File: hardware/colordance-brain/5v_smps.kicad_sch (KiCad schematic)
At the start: 15 parts, among them J14 Anderson, U8 AP3211

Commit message: Start updating brain for v1.2
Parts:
- J14: footprint homebrew:Anderson_1336G1_right_angle_bottom_two -> Homebrew:Anderson_1336G1_right_angle_bottom_two
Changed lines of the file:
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@@
       (effects (font (size 1.524 1.524)))
     )
-    (property "Footprint" "homebrew:Anderson_1336G1_right_angle_bottom_two" (id 2) (at 33.02 50.8 0)
+    (property "Footprint" "Homebrew:Anderson_1336G1_right_angle_bottom_two" (id 2) (at 33.02 50.8 0)
       (effects (font (size 1.524 1.524)) hide)
     )

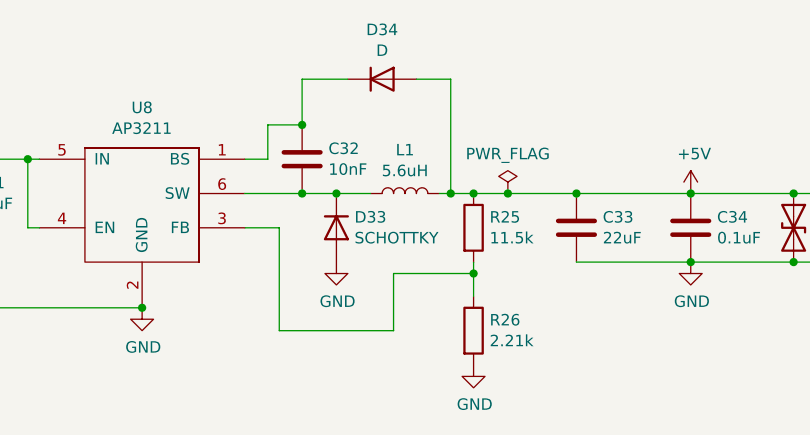
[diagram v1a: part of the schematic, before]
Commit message: Update colordance-brain PCB files to KiCAD 7
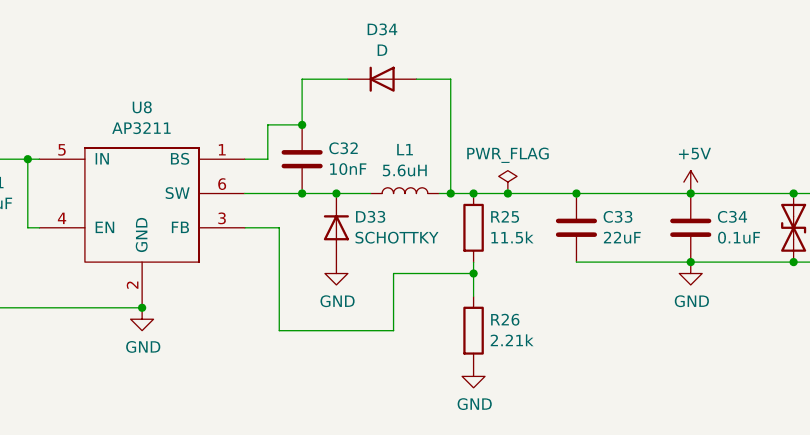
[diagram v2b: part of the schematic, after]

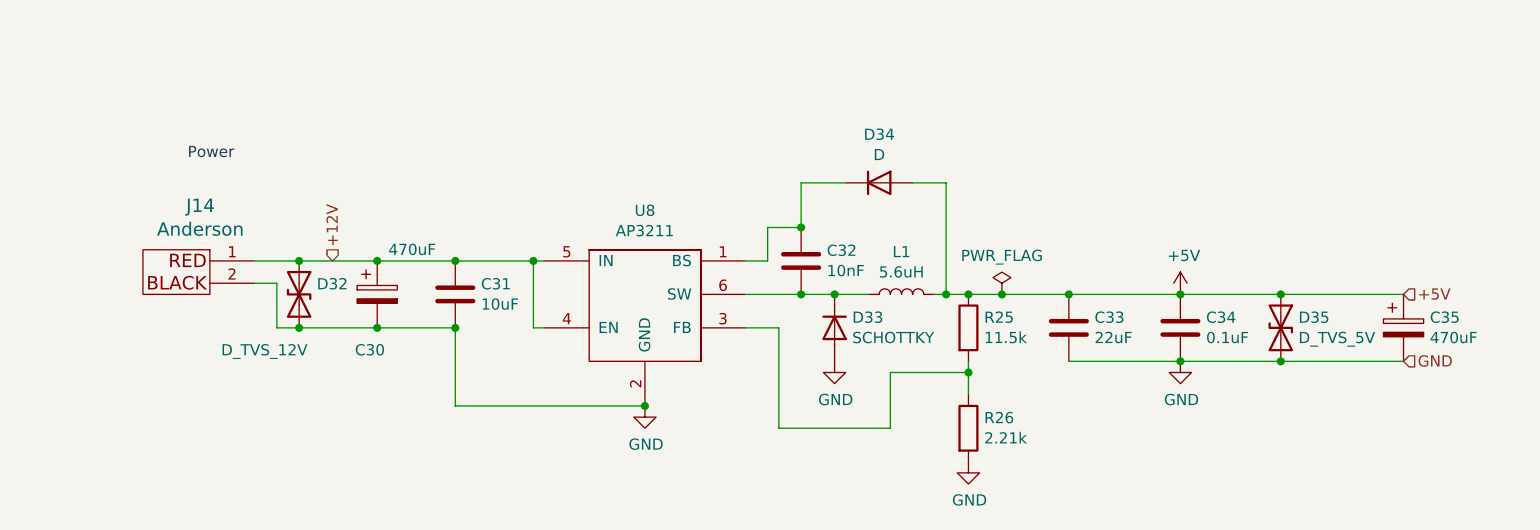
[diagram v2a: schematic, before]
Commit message: Update colordance-brain schematic for v1.3: JLC assembly
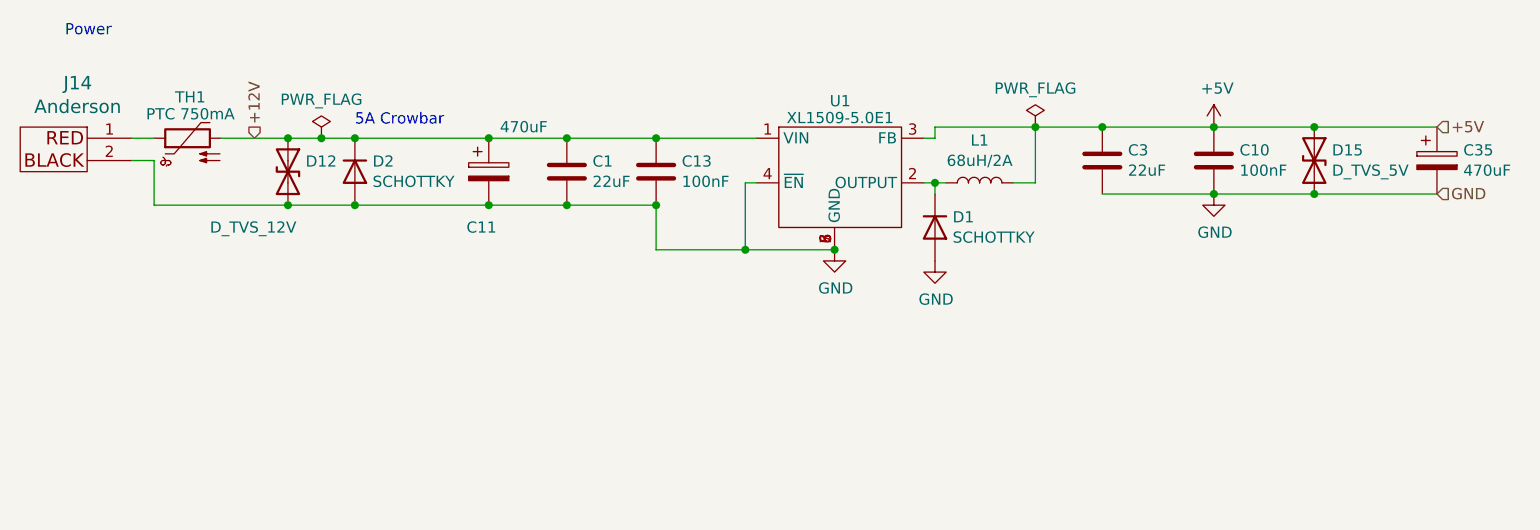
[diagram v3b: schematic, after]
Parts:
- removed C30: 470uF, Capacitor_THT:CP_Radial_D10.0mm_P5.00mm, symbol Device:CP
- removed C31: 10uF, Capacitor_SMD:C_0805_2012Metric, symbol Device:C
- removed C32: 10nF, Capacitor_SMD:C_0603_1608Metric, symbol Device:C
- removed C33: 22uF, Capacitor_SMD:C_0805_2012Metric, symbol Device:C
- removed C34: 0.1uF, Capacitor_SMD:C_0603_1608Metric, symbol Device:C
- removed D32: D_TVS_12V, Diode_SMD:D_SMB, symbol Device:D_TVS
- removed D33: SCHOTTKY, Diode_SMD:D_SOD-123, symbol Device:D
- removed D34: D, Diode_SMD:D_SOD-323, symbol Device:D
- removed D35: D_TVS_5V, Diode_SMD:D_SMB, symbol Device:D_TVS
- removed R25: 11.5k, Resistor_SMD:R_0603_1608Metric, symbol Device:R
- removed R26: 2.21k, Resistor_SMD:R_0603_1608Metric, symbol Device:R
- removed U8: AP3211, Package_TO_SOT_SMD:SOT-23-6, symbol colordance-brain-rescue:AP3211-Homebrew
- added C1, C3: 22uF, Capacitor_SMD:C_0805_2012Metric, symbol Device:C
- added C10, C13: 100nF, Capacitor_SMD:C_0402_1005Metric, symbol Device:C
- added C11: 470uF, Capacitor_THT:CP_Radial_D10.0mm_P5.00mm, symbol Device:C_Polarized
- added D1, D2: SCHOTTKY, Diode_SMD:D_SMA, symbol Device:D
- added D12: D_TVS_12V, Diode_SMD:D_SMB, symbol Device:D_TVS
- added D15: D_TVS_5V, Diode_SMD:D_SMB, symbol Device:D_TVS
- added TH1: PTC 750mA, Fuse:Fuse_1812_4532Metric, symbol Device:Thermistor_PTC
- added U1: XL1509-5.0E1, Package_SO:SOIC-8_5.23x5.23mm_P1.27mm, symbol Homebrew:XL1509-5.0E1
- J14: symbol colordance-brain-rescue:Anderson_two_redblack_src-Homebrew -> Homebrew:Anderson_two_redblack_src
- L1: value 5.6uH -> 68uH/2A; footprint Inductor_SMD:L_Taiyo-Yuden_NR-60xx -> Homebrew:L_PROD-Tech_PSPMAA0805; LCSC (none) -> C2962891; MPN NR6028T6R0M -> (none)
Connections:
- net +12V: now also C1.1, C11.1, C13.1, D12.1 (A1), D2.1 (K), TH1.2, U1.1 (VIN); no longer J14.1
- net +5V: now also C10.1, C3.1, D15.1 (A1), U1.3 (FB)
- net GND: now also C1.2, C10.2, C11.2, C13.2, C3.2, D1.2 (A), D12.2 (A2), D15.2 (A2), D2.2 (A), U1.4 (~{EN}), U1.5 (GND), U1.6 (GND), U1.7 (GND), U1.8 (GND)
- net at L1.1: now also D1.1 (K), U1.2 (OUTPUT)
- new net: J14.1, TH1.1
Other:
- note added: "5A Crowbar"
- moved on the sheet: C35, J14

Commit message: Update colordance-brain to 1.3: JLC assembly (completed)
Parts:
- renumbered C11 to C30, C1 to C31, C13 to C32, C3 to C33, C10 to C34, D12 to D32, D2 to D33, D1 to D34, D15 to D35, U1 to U8
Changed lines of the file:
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@@
   (symbol (lib_id "power:GND") (at 106.68 44.45 0) (unit 1)
     (in_bom yes) (on_board yes) (dnp no)
-    (property "Reference" "#PWR0101" (at 106.68 50.8 0)
+    (property "Reference" "#PWR0107" (at 106.68 50.8 0)
       (effects (font (size 1.27 1.27)) hide)
     )
@@
   (symbol (lib_name "D_1") (lib_id "Device:D") (at 118.11 41.91 270) (unit 1)
     (in_bom yes) (on_board yes) (dnp no)
-    (property "Reference" "D1" (at 120.1166 40.7416 90)
+    (property "Reference" "D34" (at 120.1166 40.7416 90)
       (effects (font (size 1.27 1.27)) (justify left))
     )
@@
   (symbol (lib_id "power:GND") (at 118.11 45.72 0) (unit 1)
     (in_bom yes) (on_board yes) (dnp no)
-    (property "Reference" "#PWR0102" (at 118.11 52.07 0)
+    (property "Reference" "#PWR0106" (at 118.11 52.07 0)
       (effects (font (size 1.27 1.27)) hide)
     )
@@
   (symbol (lib_id "Device:C") (at 137.16 34.29 0) (unit 1)
     (in_bom yes) (on_board yes) (dnp no)
-    (property "Reference" "C3" (at 140.081 33.1216 0)
+    (property "Reference" "C33" (at 140.081 33.1216 0)
       (effects (font (size 1.27 1.27)) (justify left))
     )
@@
   (symbol (lib_id "Device:D_TVS") (at 44.45 35.56 270) (unit 1)
     (in_bom yes) (on_board yes) (dnp no)
-    (property "Reference" "D12" (at 46.4566 34.3916 90)
+    (property "Reference" "D32" (at 46.4566 34.3916 90)
       (effects (font (size 1.27 1.27)) (justify left))
     )
@@
   (symbol (lib_id "Device:C") (at 149.86 34.29 0) (unit 1)
     (in_bom yes) (on_board yes) (dnp no)
-    (property "Reference" "C10" (at 152.781 33.1216 0)
+    (property "Reference" "C34" (at 152.781 33.1216 0)
       (effects (font (size 1.27 1.27)) (justify left))
     )
@@
   (symbol (lib_id "Device:D_TVS") (at 161.29 34.29 270) (unit 1)
     (in_bom yes) (on_board yes) (dnp no)
-    (property "Reference" "D15" (at 163.2966 33.1216 90)
+    (property "Reference" "D35" (at 163.2966 33.1216 90)
       (effects (font (size 1.27 1.27)) (justify left))
     )
@@
   (symbol (lib_id "Device:C_Polarized") (at 67.31 35.56 0) (unit 1)
     (in_bom yes) (on_board yes) (dnp no)
-    (property "Reference" "C11" (at 64.77 41.91 0)
+    (property "Reference" "C30" (at 64.77 41.91 0)
       (effects (font (size 1.27 1.27)) (justify left))
     )
@@
   (symbol (lib_id "Device:C") (at 86.36 35.56 0) (unit 1)
     (in_bom yes) (on_board yes) (dnp no)
-    (property "Reference" "C13" (at 89.281 34.3916 0)
+    (property "Reference" "C32" (at 89.281 34.3916 0)
       (effects (font (size 1.27 1.27)) (justify left))
     )
@@
   (symbol (lib_name "D_2") (lib_id "Device:D") (at 52.07 35.56 270) (unit 1)
     (in_bom yes) (on_board yes) (dnp no)
-    (property "Reference" "D2" (at 54.0766 34.3916 90)
+    (property "Reference" "D33" (at 54.0766 34.3916 90)
       (effects (font (size 1.27 1.27)) (justify left))
     )
@@
   (symbol (lib_name "PWR_FLAG_2") (lib_id "power:PWR_FLAG") (at 48.26 31.75 0) (unit 1)
     (in_bom yes) (on_board yes) (dnp no)
-    (property "Reference" "#FLG01" (at 48.26 29.845 0)
+    (property "Reference" "#FLG0101" (at 48.26 29.845 0)
       (effects (font (size 1.27 1.27)) hide)
     )
@@
   (symbol (lib_id "Homebrew:XL1509-5.0E1") (at 105.41 34.29 0) (unit 1)
     (in_bom yes) (on_board yes) (dnp no) (fields_autoplaced)
-    (property "Reference" "U1" (at 107.315 27.5209 0)
+    (property "Reference" "U8" (at 107.315 27.5209 0)
       (effects (font (size 1.27 1.27)))
     )
@@
   (symbol (lib_id "Device:C") (at 76.2 35.56 0) (unit 1)
     (in_bom yes) (on_board yes) (dnp no)
-    (property "Reference" "C1" (at 79.121 34.3916 0)
-      (effects (font (size 1.27 1.27)) (justify left))
-    )
+    (property "Reference" "C31" (at 79.121 34.3916 0)
+      (effects (font (size 1.27 1.27)) (justify left))
+    )

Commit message: Fix colordance-brain v1.3 footprint for XL1509 SMPS
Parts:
- U8: footprint Package_SO:SOIC-8_5.23x5.23mm_P1.27mm -> Package_SO:SOIC-8_3.9x4.9mm_P1.27mm
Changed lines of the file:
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@@
       (effects (font (size 1.27 1.27)))
     )
-    (property "Footprint" "Package_SO:SOIC-8_5.23x5.23mm_P1.27mm" (at 105.41 27.94 0)
+    (property "Footprint" "Package_SO:SOIC-8_3.9x4.9mm_P1.27mm" (at 105.41 27.94 0)
       (effects (font (size 1.27 1.27)) hide)
     )
